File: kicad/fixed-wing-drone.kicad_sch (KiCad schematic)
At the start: 24 parts, among them J1 SERVO1, J10 ACC POWER, J11 RC_POWER_OUT, J12 AIRSPEED JST SH, J13 EXTRA STEMMA QT, J14 BAROMETER JST SH, J15 IMU JST SH, J16 ACC IO, J17 FC UBEC Input, J18 ESC UBEC Input, J19 Secondary ESC Input, J2 SERVO2, J3 SERVO3, J4 SERVO4, J5 SERVO5, J6 SERVO6, J7 RC_SIGNAL_IN, J8 LIDAR UART, J9 GPS UART, Q1 FC REV POLARITY PROT, Q2 ESC REV POLARITY PROT, U1 ESP32-S3-DevKitC

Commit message: updated gitignore and tried out some changes to pcb layout
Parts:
- added J20: LIDAR BKUP, Connector_PinHeader_2.54mm:PinHeader_1x04_P2.54mm_Vertical, symbol Connector:Conn_01x04_Pin
- J1: value SERVO1 -> 1; footprint Connector_PinHeader_2.54mm:PinHeader_1x03_P2.54mm_Vertical -> Connector_PinHeader_2.54mm:PinHeader_1x03_P2.54mm_Vertical_SMD_Pin1Left
- J11: footprint Connector_PinHeader_2.54mm:PinHeader_1x02_P2.54mm_Vertical -> Connector_PinHeader_2.54mm:PinHeader_1x02_P2.54mm_Vertical_SMD_Pin1Left
- J12: value AIRSPEED JST SH -> I2C
- J14: value BAROMETER JST SH -> I2C
- J15: value IMU JST SH -> I2C
- J17, J18, J19: footprint Connector_PinHeader_2.54mm:PinHeader_1x03_P2.54mm_Vertical -> Connector_PinHeader_2.54mm:PinHeader_1x03_P2.54mm_Vertical_SMD_Pin1Left
- J2: value SERVO2 -> 2; footprint Connector_PinHeader_2.54mm:PinHeader_1x03_P2.54mm_Vertical -> Connector_PinHeader_2.54mm:PinHeader_1x03_P2.54mm_Vertical_SMD_Pin1Left
- J3: value SERVO3 -> 3; footprint Connector_PinHeader_2.54mm:PinHeader_1x03_P2.54mm_Vertical -> Connector_PinHeader_2.54mm:PinHeader_1x03_P2.54mm_Vertical_SMD_Pin1Left
- J4: value SERVO4 -> 4; footprint Connector_PinHeader_2.54mm:PinHeader_1x03_P2.54mm_Vertical -> Connector_PinHeader_2.54mm:PinHeader_1x03_P2.54mm_Vertical_SMD_Pin1Left
- J5: value SERVO5 -> 5; footprint Connector_PinHeader_2.54mm:PinHeader_1x03_P2.54mm_Vertical -> Connector_PinHeader_2.54mm:PinHeader_1x03_P2.54mm_Vertical_SMD_Pin1Left
- J6: value SERVO6 -> 6; footprint Connector_PinHeader_2.54mm:PinHeader_1x03_P2.54mm_Vertical -> Connector_PinHeader_2.54mm:PinHeader_1x03_P2.54mm_Vertical_SMD_Pin1Left
- J7: footprint Connector_PinHeader_2.54mm:PinHeader_1x06_P2.54mm_Vertical -> Connector_PinHeader_2.54mm:PinHeader_1x06_P2.54mm_Vertical_SMD_Pin1Left
- J8: value LIDAR UART -> LIDAR; footprint Connector_PinHeader_2.54mm:PinHeader_1x04_P2.54mm_Vertical -> Connector_Molex:Molex_PicoBlade_53398-0471_1x04-1MP_P1.25mm_Vertical
- J9: value GPS UART -> GPS; footprint Connector_PinHeader_2.54mm:PinHeader_1x04_P2.54mm_Vertical -> Connector_PinHeader_2.54mm:PinHeader_1x04_P2.54mm_Vertical_SMD_Pin1Left
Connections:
- net +3V3: now also J9.1 (Pin_1); no longer J8.2 (Pin_2), J9.2 (Pin_2)
- net FC_5v: now also J8.1 (Pin_1), J20.1 (Pin_1)
- net GND: now also J17.3 (Pin_3), J18.3 (Pin_3), J19.3 (Pin_3), J8.4 (Pin_4), J9.2 (Pin_2), J20.4 (Pin_4); no longer J17.2 (Pin_2), J18.2 (Pin_2), J19.2 (Pin_2), J8.1 (Pin_1), J9.1 (Pin_1)
- net LIDAR_RX: now also J8.3 (Pin_3), J20.3 (Pin_3); no longer J8.4 (Pin_4)
- net LIDAR_TX: now also J8.2 (Pin_2), J20.2 (Pin_2); no longer J8.3 (Pin_3)
- net at Q1.2: now also J17.2 (Pin_2); no longer J17.3 (Pin_3)
- net at Q2.2: now also J18.2 (Pin_2); no longer J18.3 (Pin_3)

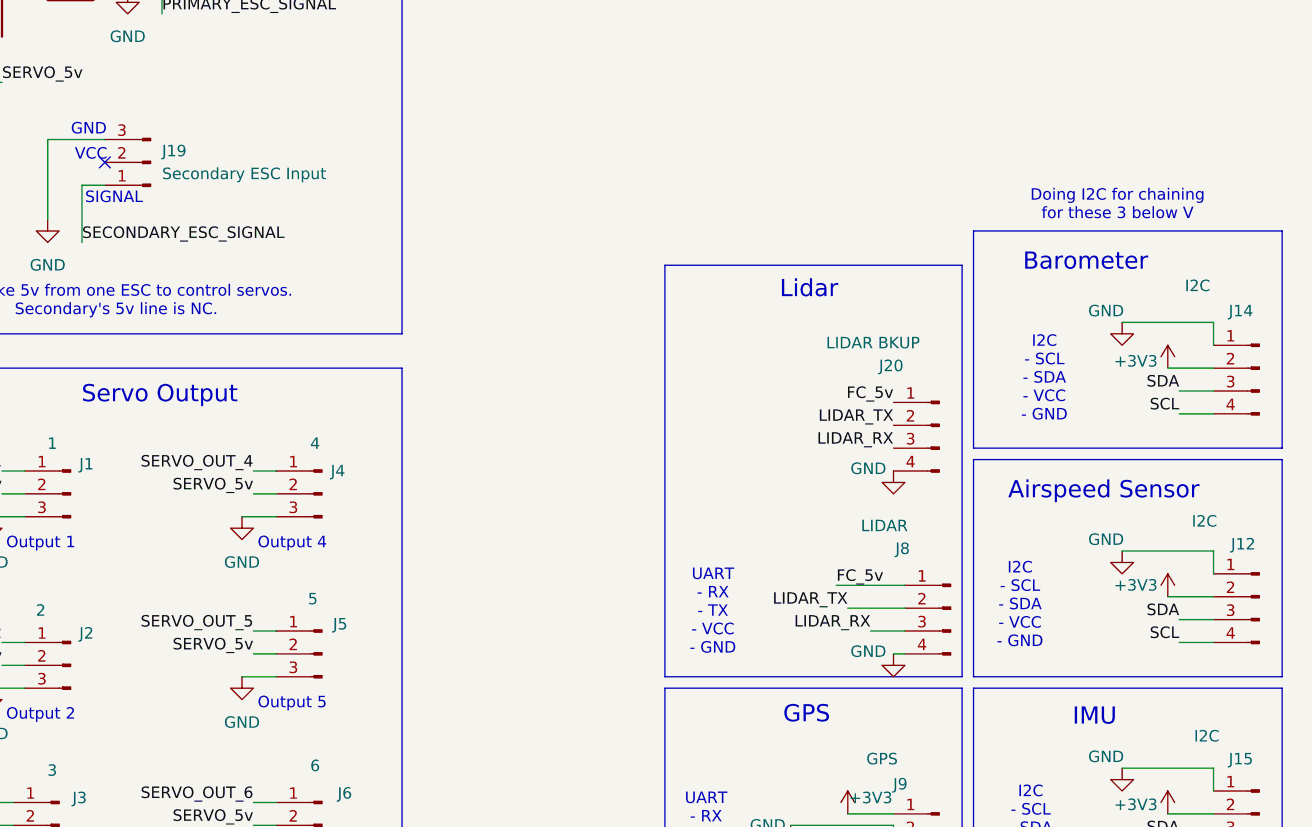
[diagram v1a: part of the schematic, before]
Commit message: V2 PCB; Fixed pin ordering, changed to mostly smd connectors, added 5v jst gh for lidar & airspeed; and fixed misprints on silkscreen
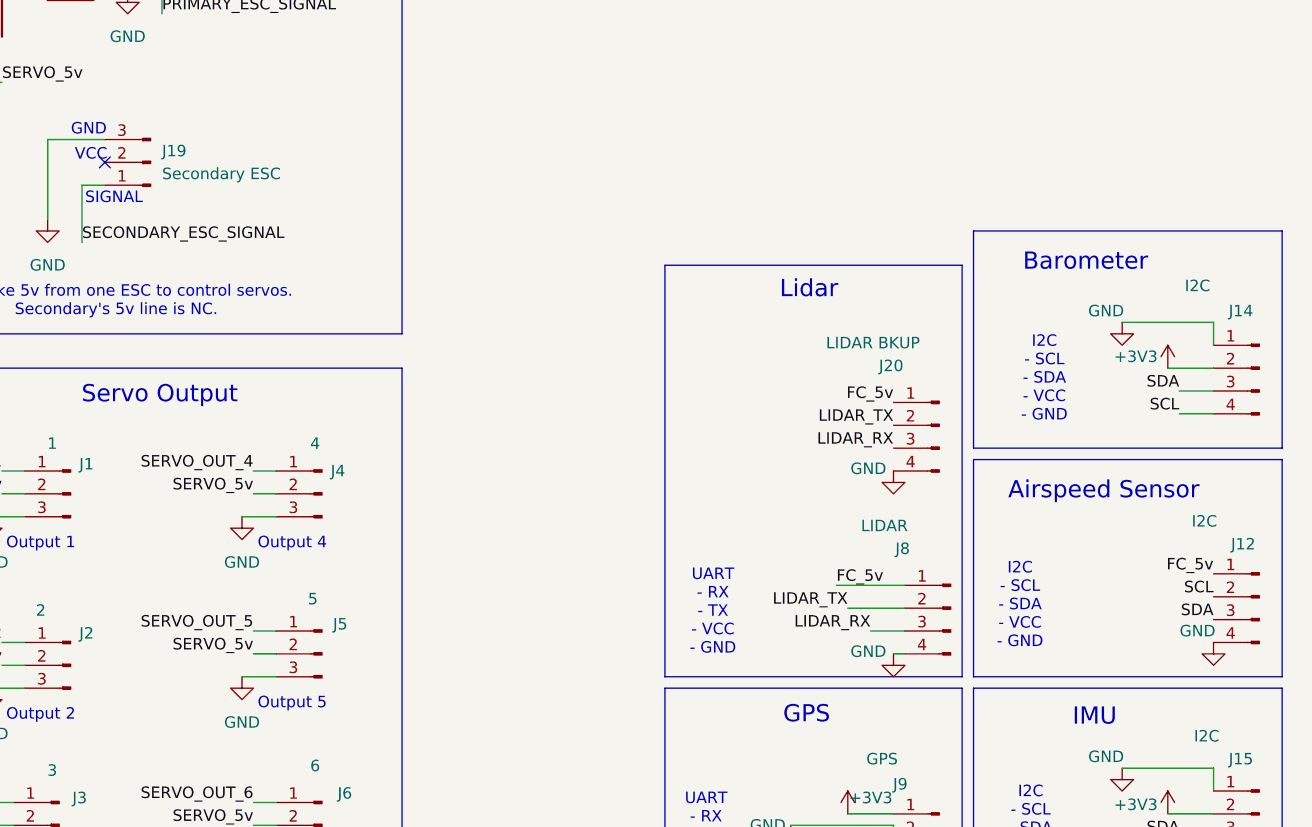
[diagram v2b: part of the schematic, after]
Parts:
- J12: footprint Connector_JST:JST_SH_BM04B-SRSS-TB_1x04-1MP_P1.00mm_Vertical -> Connector_JST:JST_GH_BM04B-GHS-TBT_1x04-1MP_P1.25mm_Vertical
- J19: value Secondary ESC Input -> Secondary ESC
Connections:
- net +3V3: no longer J12.2 (Pin_2)
- net FC_5v: now also J12.1 (Pin_1)
- net GND: now also J12.4 (Pin_4); no longer J12.1 (Pin_1)
- net SCL: now also J12.2 (Pin_2); no longer J12.4 (Pin_4)
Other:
- note removed: "Doing I2C for chaining for these 3 below V"
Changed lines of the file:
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@@
 		)
 	)
-	(text "Doing I2C for chaining\nfor these 3 below V"
-		(exclude_from_sim no)
-		(at 258.572 82.296 0)
-		(effects
-			(font
-				(size 1.27 1.27)
-			)
-		)
-	)
 	(text "Accessory I/O"
 		(exclude_from_sim no)
@@
 	(wire
 		(pts
-			(xy 264.16 125.73) (xy 269.24 125.73)
-		)
-		(stroke
-			(width 0)
-			(type default)
-		)
-	)
-	(wire
-		(pts
 			(xy 146.05 74.93) (xy 139.7 74.93)
 		)
@@
 	(wire
 		(pts
-			(xy 265.43 128.27) (xy 269.24 128.27)
-		)
-		(stroke
-			(width 0)
-			(type default)
-		)
-	)
-	(wire
-		(pts
 			(xy 266.7 40.64) (xy 269.24 40.64)
 		)
@@
 	(wire
 		(pts
-			(xy 269.24 120.65) (xy 269.24 123.19)
-		)
-		(stroke
-			(width 0)
-			(type default)
-		)
-	)
-	(wire
-		(pts
 			(xy 241.3 38.1) (xy 245.11 38.1)
 		)
@@
 	(wire
 		(pts
-			(xy 265.43 130.81) (xy 269.24 130.81)
-		)
-		(stroke
-			(width 0)
-			(type default)
-		)
-	)
-	(wire
-		(pts
 			(xy 265.43 154.94) (xy 269.24 154.94)
 		)
@@
 	(wire
 		(pts
-			(xy 259.08 120.65) (xy 269.24 120.65)
-		)
-		(stroke
-			(width 0)
-			(type default)
-		)
-	)
-	(wire
-		(pts
 			(xy 227.33 124.46) (xy 234.95 124.46)
 		)
@@
 		)
 	)
+	(label "FC_5v"
+		(at 269.24 123.19 180)
+		(effects
+			(font
+				(size 1.27 1.27)
+			)
+			(justify right bottom)
+		)
+	)
 	(label "SECONDARY_ESC_SIGNAL"
 		(at 143.51 86.36 0)
@@
 	)
 	(label "SCL"
-		(at 265.43 130.81 180)
+		(at 269.24 125.73 180)
 		(effects
 			(font
@@
 	)
 	(label "SDA"
-		(at 265.43 128.27 180)
+		(at 269.24 128.27 180)
 		(effects
 			(font
@@
 	(symbol
 		(lib_id "power:GND")
-		(at 259.08 120.65 0)
+		(at 269.24 130.81 0)
 		(unit 1)
 		(body_style 1)
@@
 		(dnp no)
 		(property "Reference" "#PWR014"
-			(at 259.08 127 0)
+			(at 269.24 137.16 0)
 			(hide yes)
 			(show_name no)
@@
 		)
 		(property "Value" "GND"
-			(at 257.302 119.38 0)
+			(at 267.462 129.54 0)
 			(show_name no)
 			(do_not_autoplace no)
@@
 		)
 		(property "Footprint" ""
-			(at 259.08 120.65 0)
+			(at 269.24 130.81 0)
 			(hide yes)
 			(show_name no)
@@
 		)
 		(property "Datasheet" ""
-			(at 259.08 120.65 0)
+			(at 269.24 130.81 0)
 			(hide yes)
 			(show_name no)
@@
 		)
 		(property "Description" "Power symbol creates a global label with name \"GND\" , ground"
-			(at 259.08 120.65 0)
+			(at 269.24 130.81 0)
 			(hide yes)
 			(show_name no)
@@
 	(symbol
 		(lib_id "power:+3V3")
-		(at 264.16 125.73 0)
+		(at 264.16 100.33 0)
 		(unit 1)
 		(body_style 1)
@@
 		(dnp no)
 		(property "Reference" "#PWR018"
-			(at 264.16 129.54 0)
+			(at 264.16 104.14 0)
 			(hide yes)
 			(show_name no)
@@
 		)
 		(property "Value" "+3V3"
-			(at 260.604 124.46 0)
+			(at 260.604 99.06 0)
 			(show_name no)
 			(do_not_autoplace no)
@@
 		)
 		(property "Footprint" ""
-			(at 264.16 125.73 0)
+			(at 264.16 100.33 0)
 			(hide yes)
 			(show_name no)
@@
 		)
 		(property "Datasheet" ""
-			(at 264.16 125.73 0)
+			(at 264.16 100.33 0)
 			(hide yes)
 			(show_name no)
@@
 		)
 		(property "Description" "Power symbol creates a global label with name \"+3V3\""
-			(at 264.16 125.73 0)
+			(at 264.16 100.33 0)
 			(hide yes)
 			(show_name no)
@@
 			)
 		)
-		(property "Value" "Secondary ESC Input"
+		(property "Value" "Secondary ESC"
 			(at 152.4 78.7399 0)
 			(show_name no)
@@
 			)
 		)
-		(property "Footprint" "Connector_JST:JST_SH_BM04B-SRSS-TB_1x04-1MP_P1.00mm_Vertical"
+		(property "Footprint" "Connector_JST:JST_GH_BM04B-GHS-TBT_1x04-1MP_P1.25mm_Vertical"
 			(at 274.32 125.73 0)
 			(hide yes)
@@
 					(unit 1)
 				)
-			)
-		)
-	)
-	(symbol
-		(lib_id "power:+3V3")
-		(at 264.16 100.33 0)
-		(unit 1)
-		(body_style 1)
-		(exclude_from_sim no)
-		(in_bom yes)
-		(on_board yes)
-		(in_pos_files yes)
-		(dnp no)
-		(property "Reference" "#PWR022"
-			(at 264.16 104.14 0)
-			(hide yes)
-			(show_name no)
-			(do_not_autoplace no)
-			(effects
-				(font
-					(size 1.27 1.27)
-				)
-			)
-		)
-		(property "Value" "+3V3"
-			(at 260.604 99.568 0)
-			(show_name no)
-			(do_not_autoplace no)
-			(effects
-				(font
-					(size 1.27 1.27)
-				)
-			)
-		)
-		(property "Footprint" ""
-			(at 264.16 100.33 0)
-			(hide yes)
-			(show_name no)
-			(do_not_autoplace no)
-			(effects
-				(font
-					(size 1.27 1.27)
-				)
-			)
-		)
-		(property "Datasheet" ""
-			(at 264.16 100.33 0)
-			(hide yes)
-			(show_name no)
-			(do_not_autoplace no)
-			(effects
-				(font
-					(size 1.27 1.27)
-				)
-			)
-		)
-		(property "Description" "Power symbol creates a global label with name \"+3V3\""
-			(at 264.16 100.33 0)
-			(hide yes)
-			(show_name no)
-			(do_not_autoplace no)
-			(effects
-				(font
-					(size 1.27 1.27)
-				)
-			)
-		)
-		(pin "1"
-		)
-		(instances
-			(project "fixed-wing-drone"
-				(path "/6fbedc8c-8b3e-4075-8dcf-52085fc3223b"
-					(reference "#PWR022")
-					(unit 1)
-				)

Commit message: Reverted to through hole but added new connectors for airspeed and added 5v for powering it. Did other minor revisions like removing some of the extra AUX IO
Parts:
- removed J16: ACC IO, Connector_PinHeader_2.54mm:PinHeader_1x10_P2.54mm_Vertical, symbol Connector:Conn_01x10_Pin
- added J21: AUX, Connector_PinHeader_2.54mm:PinHeader_1x07_P2.54mm_Vertical, symbol Connector:Conn_01x07_Pin
- J1, J17, J18, J19, J2, J3, J4, J5, J6: footprint Connector_PinHeader_2.54mm:PinHeader_1x03_P2.54mm_Vertical_SMD_Pin1Left -> Connector_PinHeader_2.54mm:PinHeader_1x03_P2.54mm_Vertical; now left out of the parts list
- J10, J20, U1: now left out of the parts list
- J11: value RC_POWER_OUT -> RC POWER; footprint Connector_PinHeader_2.54mm:PinHeader_1x02_P2.54mm_Vertical_SMD_Pin1Left -> Connector_PinHeader_2.54mm:PinHeader_1x02_P2.54mm_Vertical; now left out of the parts list
- J12: value I2C -> Airspeed I2C; LCSC Part # (none) -> C161692
- J13: LCSC Part # (none) -> C160390
- J14, J15: value I2C -> QT I2C; LCSC Part # (none) -> C160390
- J7: value RC_SIGNAL_IN -> RC SIGNAL IN; footprint Connector_PinHeader_2.54mm:PinHeader_1x06_P2.54mm_Vertical_SMD_Pin1Left -> Connector_PinHeader_2.54mm:PinHeader_1x06_P2.54mm_Vertical; now left out of the parts list
- J8: LCSC Part # (none) -> C234195
- J9: footprint Connector_PinHeader_2.54mm:PinHeader_1x04_P2.54mm_Vertical_SMD_Pin1Left -> Connector_PinHeader_2.54mm:PinHeader_1x04_P2.54mm_Vertical; now left out of the parts list
- Q1, Q2: LCSC Part # (none) -> C15155
- R1, R2: footprint Resistor_SMD:R_0201_0603Metric_Pad0.64x0.40mm_HandSolder -> Resistor_SMD:R_0402_1005Metric; LCSC Part # (none) -> C25741
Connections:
- net ACC_7 is gone; now on net RECIEVER_5: U1.7 (GPIO7/ADC1_CH6)
- net ACC_8 is gone; now on net RECIEVER_6: U1.12 (GPIO8/ADC1_CH7)
- net ACC_9 is gone; now on net RECIEVER_1: U1.15 (GPIO9/ADC1_CH8)
- net ACC_0: now also J21.1 (Pin_1)
- net ACC_1: now also J21.2 (Pin_2)
- net ACC_2: now also J21.3 (Pin_3)
- net ACC_3: now also J21.4 (Pin_4)
- net ACC_4: now also J21.5 (Pin_5)
- net ACC_5: now also J21.6 (Pin_6)
- net ACC_6: now also J21.7 (Pin_7)
- net RECIEVER_1: no longer U1.34 (GPIO37)
- net RECIEVER_5: no longer U1.32 (GPIO35)
- net RECIEVER_6: no longer U1.33 (GPIO36)

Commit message: opened file n now i need to repush
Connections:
- net GND: no longer U1.22 (GND), U1.23 (GND), U1.24 (GND), U1.44 (GND)
- net SERVO_OUT_2: no longer J2.1 (Pin_1)
- net SERVO_OUT_5: no longer J5.1 (Pin_1)
- new net: U1.22 (GND), U1.23 (GND), U1.24 (GND), U1.44 (GND)
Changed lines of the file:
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@@
 	)
 	(rectangle
-		(start 17.78 17.78)
-		(end 113.03 135.89)
-		(stroke
-			(width 0)
-			(type default)
-		)
-		(fill
-			(type none)
-		)
-	)
-	(rectangle
 		(start 242.57 85.09)
 		(end 276.86 109.22)
@@
 		)
 	)
-	(rectangle
-		(start 118.11 100.33)
-		(end 179.07 160.02)
-		(stroke
-			(width 0)
-			(type default)
-		)
-		(fill
-			(type none)
-		)
-	)
 	(text "Extra Stemma QT port"
 		(exclude_from_sim no)
@@
 	(wire
 		(pts
-			(xy 67.31 121.92) (xy 67.31 125.73)
-		)
-		(stroke
-			(width 0)
-			(type default)
-		)
-	)
-	(wire
-		(pts
 			(xy 132.08 30.48) (xy 154.94 30.48)
 		)
@@
 		)
 	)
-	(label "SERVO_OUT_2"
-		(at 134.62 130.81 180)
-		(effects
-			(font
-				(size 1.27 1.27)
-			)
-			(justify right bottom)
-		)
-	)
 	(label "SERVO_5v"
 		(at 162.56 132.08 180)
@@
 		)
 	)
-	(label "SERVO_OUT_5"
-		(at 162.56 129.54 180)
-		(effects
-			(font
-				(size 1.27 1.27)
-			)
-			(justify right bottom)
-		)
-	)
 	(label "SERVO_OUT_3"
 		(at 133.35 148.59 180)
@@
 		(property "Reference" "J2"
 			(at 144.018 129.794 0)
+			(hide yes)
 			(show_name no)
 			(do_not_autoplace no)
@@
 		(property "Value" "2"
 			(at 138.938 127.254 0)
+			(hide yes)
 			(show_name no)
 			(do_not_autoplace no)
@@
 		(property "Value" "ESP32-S3-DevKitC"
 			(at 69.4533 124.46 0)
+			(hide yes)
 			(show_name no)
 			(do_not_autoplace no)
@@
 		(property "Reference" "J5"
 			(at 172.212 128.778 0)
+			(hide yes)
 			(show_name no)
 			(do_not_autoplace no)
@@
 		(property "Value" "5"
 			(at 169.164 125.984 0)
+			(hide yes)
 			(show_name no)
 			(do_not_autoplace no)
@@
 					(unit 1)
 				)
-			)
-		)
-	)
-	(symbol
-		(lib_id "power:GND")
-		(at 67.31 125.73 0)
-		(unit 1)
-		(body_style 1)
-		(exclude_from_sim no)
-		(in_bom yes)
-		(on_board yes)
-		(in_pos_files yes)
-		(dnp no)
-		(fields_autoplaced yes)
-		(property "Reference" "#PWR08"
-			(at 67.31 132.08 0)
-			(hide yes)
-			(show_name no)
-			(do_not_autoplace no)
-			(effects
-				(font
-					(size 1.27 1.27)
-				)
-			)
-		)
-		(property "Value" "GND"
-			(at 67.31 130.81 0)
-			(show_name no)
-			(do_not_autoplace no)
-			(effects
-				(font
-					(size 1.27 1.27)
-				)
-			)
-		)
-		(property "Footprint" ""
-			(at 67.31 125.73 0)
-			(hide yes)
-			(show_name no)
-			(do_not_autoplace no)
-			(effects
-				(font
-					(size 1.27 1.27)
-				)
-			)
-		)
-		(property "Datasheet" ""
-			(at 67.31 125.73 0)
-			(hide yes)
-			(show_name no)
-			(do_not_autoplace no)
-			(effects
-				(font
-					(size 1.27 1.27)
-				)
-			)
-		)
-		(property "Description" "Power symbol creates a global label with name \"GND\" , ground"
-			(at 67.31 125.73 0)
-			(hide yes)
-			(show_name no)
-			(do_not_autoplace no)
-			(effects
-				(font
-					(size 1.27 1.27)
-				)
-			)
-		)
-		(pin "1"
-		)
-		(instances
-			(project "fixed-wing-drone"
-				(path "/6fbedc8c-8b3e-4075-8dcf-52085fc3223b"
-					(reference "#PWR08")
-					(unit 1)
-				)

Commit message: PCB v3.0
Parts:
- removed J1: 1, Connector_PinHeader_2.54mm:PinHeader_1x03_P2.54mm_Vertical, symbol Connector:Conn_01x03_Pin
- removed J10: ACC POWER, Connector_PinHeader_2.54mm:PinHeader_1x04_P2.54mm_Vertical, symbol Connector:Conn_01x04_Pin
- removed J11: RC POWER, Connector_PinHeader_2.54mm:PinHeader_1x02_P2.54mm_Vertical, symbol Connector:Conn_01x02_Pin
- removed J12: Airspeed I2C, Connector_JST:JST_GH_BM04B-GHS-TBT_1x04-1MP_P1.25mm_Vertical, symbol Connector:Conn_01x04_Pin
- removed J13: EXTRA STEMMA QT, Connector_JST:JST_SH_BM04B-SRSS-TB_1x04-1MP_P1.00mm_Vertical, symbol Connector:Conn_01x04_Pin
- removed J14, J15: QT I2C, Connector_JST:JST_SH_BM04B-SRSS-TB_1x04-1MP_P1.00mm_Vertical, symbol Connector:Conn_01x04_Pin
- removed J17: FC UBEC Input, Connector_PinHeader_2.54mm:PinHeader_1x03_P2.54mm_Vertical, symbol Connector:Conn_01x03_Pin
- removed J18: ESC UBEC Input, Connector_PinHeader_2.54mm:PinHeader_1x03_P2.54mm_Vertical, symbol Connector:Conn_01x03_Pin
- removed J19: Secondary ESC, Connector_PinHeader_2.54mm:PinHeader_1x03_P2.54mm_Vertical, symbol Connector:Conn_01x03_Pin
- removed J2: 2, Connector_PinHeader_2.54mm:PinHeader_1x03_P2.54mm_Vertical, symbol Connector:Conn_01x03_Pin
- removed J20: LIDAR BKUP, Connector_PinHeader_2.54mm:PinHeader_1x04_P2.54mm_Vertical, symbol Connector:Conn_01x04_Pin
- removed J21: AUX, Connector_PinHeader_2.54mm:PinHeader_1x07_P2.54mm_Vertical, symbol Connector:Conn_01x07_Pin
- removed J3: 3, Connector_PinHeader_2.54mm:PinHeader_1x03_P2.54mm_Vertical, symbol Connector:Conn_01x03_Pin
- removed J4: 4, Connector_PinHeader_2.54mm:PinHeader_1x03_P2.54mm_Vertical, symbol Connector:Conn_01x03_Pin
- removed J5: 5, Connector_PinHeader_2.54mm:PinHeader_1x03_P2.54mm_Vertical, symbol Connector:Conn_01x03_Pin
- removed J6: 6, Connector_PinHeader_2.54mm:PinHeader_1x03_P2.54mm_Vertical, symbol Connector:Conn_01x03_Pin
- removed J7: RC SIGNAL IN, Connector_PinHeader_2.54mm:PinHeader_1x06_P2.54mm_Vertical, symbol Connector:Conn_01x06_Pin
- removed J8: LIDAR, Connector_Molex:Molex_PicoBlade_53398-0471_1x04-1MP_P1.25mm_Vertical, symbol Connector:Conn_01x04_Pin
- removed J9: GPS, Connector_PinHeader_2.54mm:PinHeader_1x04_P2.54mm_Vertical, symbol Connector:Conn_01x04_Pin
- removed Q1: FC REV POLARITY PROT, AO3407A:SOT95P280X125-3N, symbol AO3407A:AO3407A
- removed Q2: ESC REV POLARITY PROT, AO3407A:SOT95P280X125-3N, symbol AO3407A:AO3407A
- removed R1, R2: 100K, Resistor_SMD:R_0402_1005Metric, symbol Device:R
- removed U1: ESP32-S3-DevKitC, PCM_Espressif:ESP32-S3-DevKitC-trav-snf2, symbol PCM_Espressif:ESP32-S3-DevKitC
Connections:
- no-connect marks 7 -> 0
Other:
- added sheet actuator_io (servo_io.kicad_sch)
- added sheet aux (aux.kicad_sch)
- added sheet esp32s3 (esp32s3.kicad_sch)
- added sheet external_sensors (external_sensors.kicad_sch)
- added sheet fc_ldo (fc_ldo.kicad_sch)
- added sheet onboard_sensors (onboard_sensors.kicad_sch)
- note removed: "Accessory I/O"
- note removed: "Airspeed Sensor"
- note removed: "Barometer"
- note removed: "Extra Stemma QT port"
- note removed: "GND"
- note removed: "GPS"
- note removed: "I2C - SCL - SDA - VCC - GND"
- note removed: "IMU"
- note removed: "Lidar"
- note removed: "Male IO Headers"
- note removed: "Only take 5v from one ESC to control servos. Secondary's 5v line is NC."
- note removed: "Output 1"
- note removed: "Output 2"
- note removed: "Output 3"
- note removed: "Output 4"
- note removed: "Output 5"
- note removed: "Output 6"
- note removed: "Power"
- note removed: "Power Input"
- note removed: "RC Reciever"
- note removed: "Reverse polarity protection"
- note removed: "SIGNAL"
- note removed: "Servo Output"
- note removed: "Signal Lines"
- note removed: "Some exposed gpio to do simple accessory stuff like LEDs or any other things that I forgot in the rest of the pcb."
- note removed: "UART - RX - TX - VCC - GND"
- note removed: "VCC"
- note removed: "VCC / GND to Reciever"
- note removed: "uC"
